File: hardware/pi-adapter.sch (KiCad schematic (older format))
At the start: 32 parts, among them P1 CONN_01X04, P10 CONN_01X04, P11 CONN_01X04, P12 CONN_01X04, P13 CONN_01X04, P14 CONN_01X04, P15 CONN_01X04, P16 CONN_01X04, P2 CONN_01X04, P20 CONN_02X20, P21 CONN_01X03, P22 CONN_01X06, P23 CONN_01X03, P3 CONN_01X04, P30 +5V, P31 GND, P4 CONN_01X04, P5 CONN_01X04, P6 CONN_01X04, P7 CONN_01X04, P8 CONN_01X04, P9 CONN_01X04, U1 74HCT245, U2 74HCT245, U3 74HCT245, U4 74HCT245

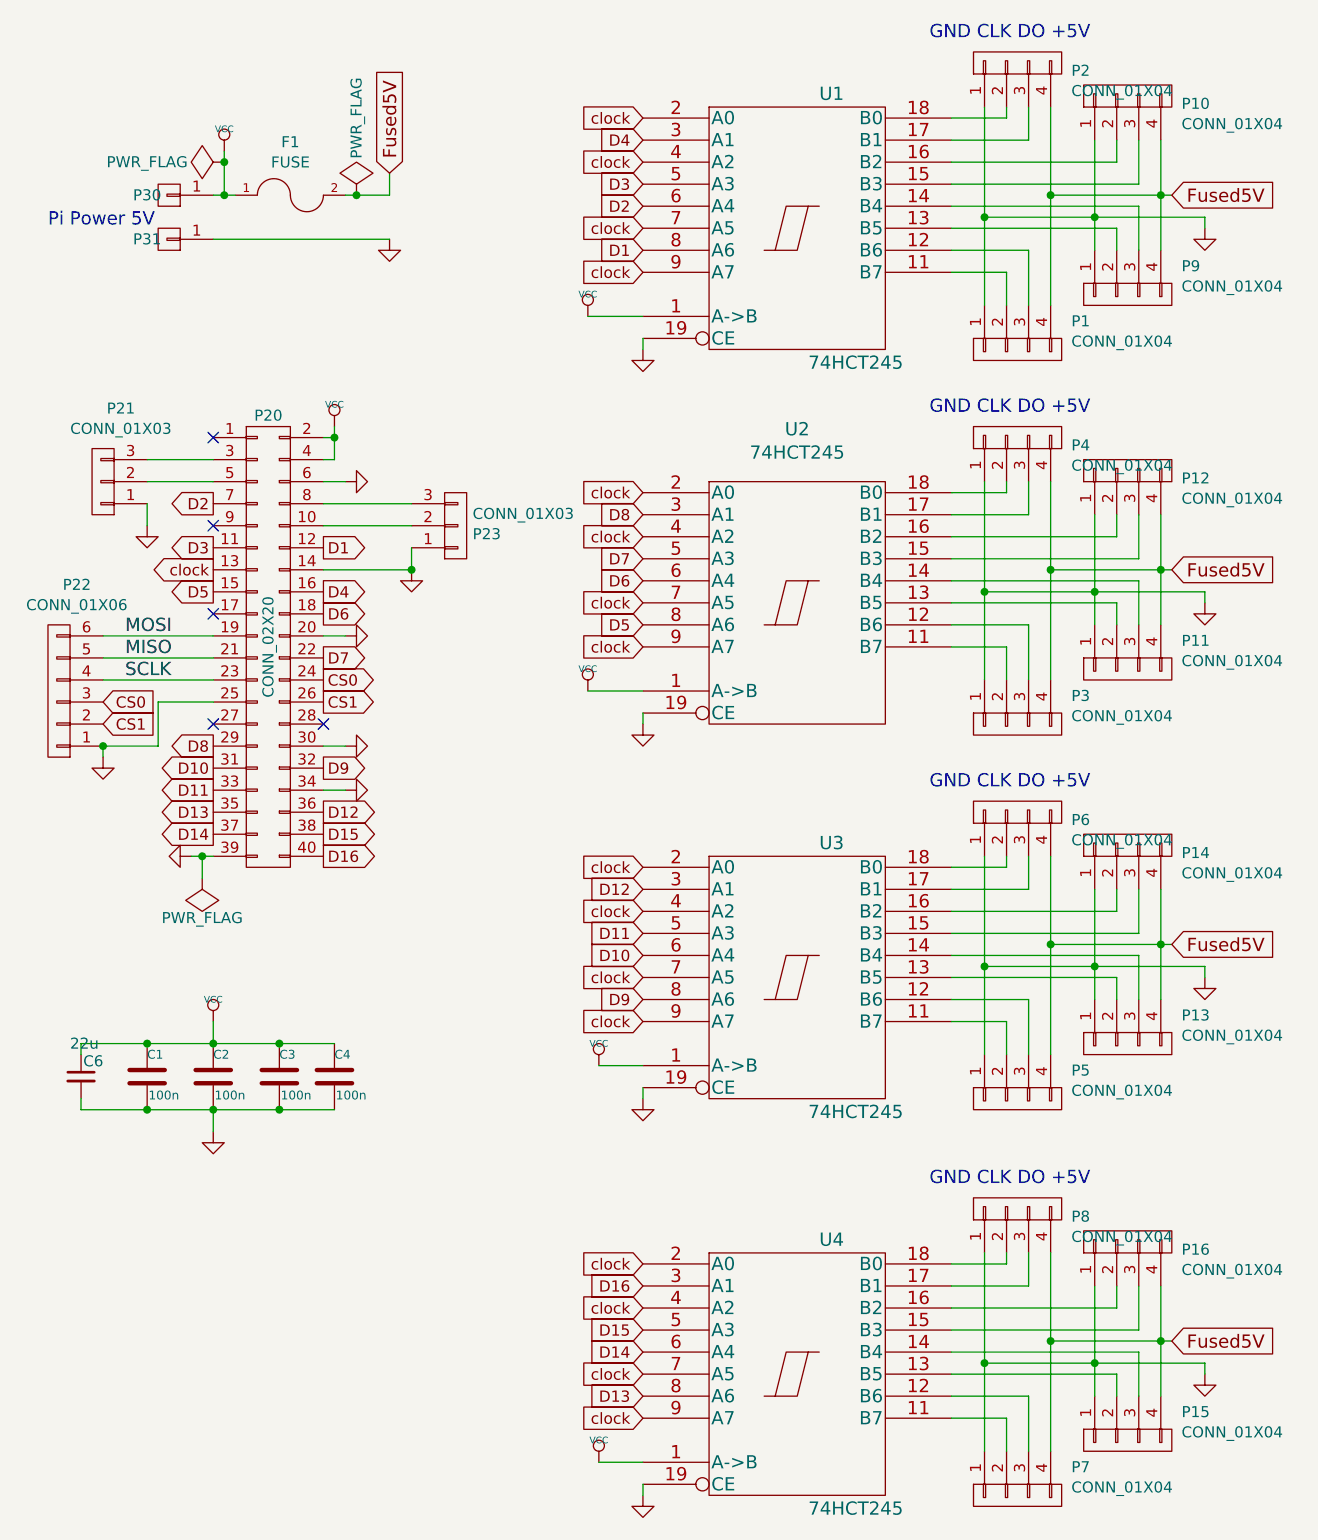
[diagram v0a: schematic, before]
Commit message: Add Schematic image in hardware/README.md
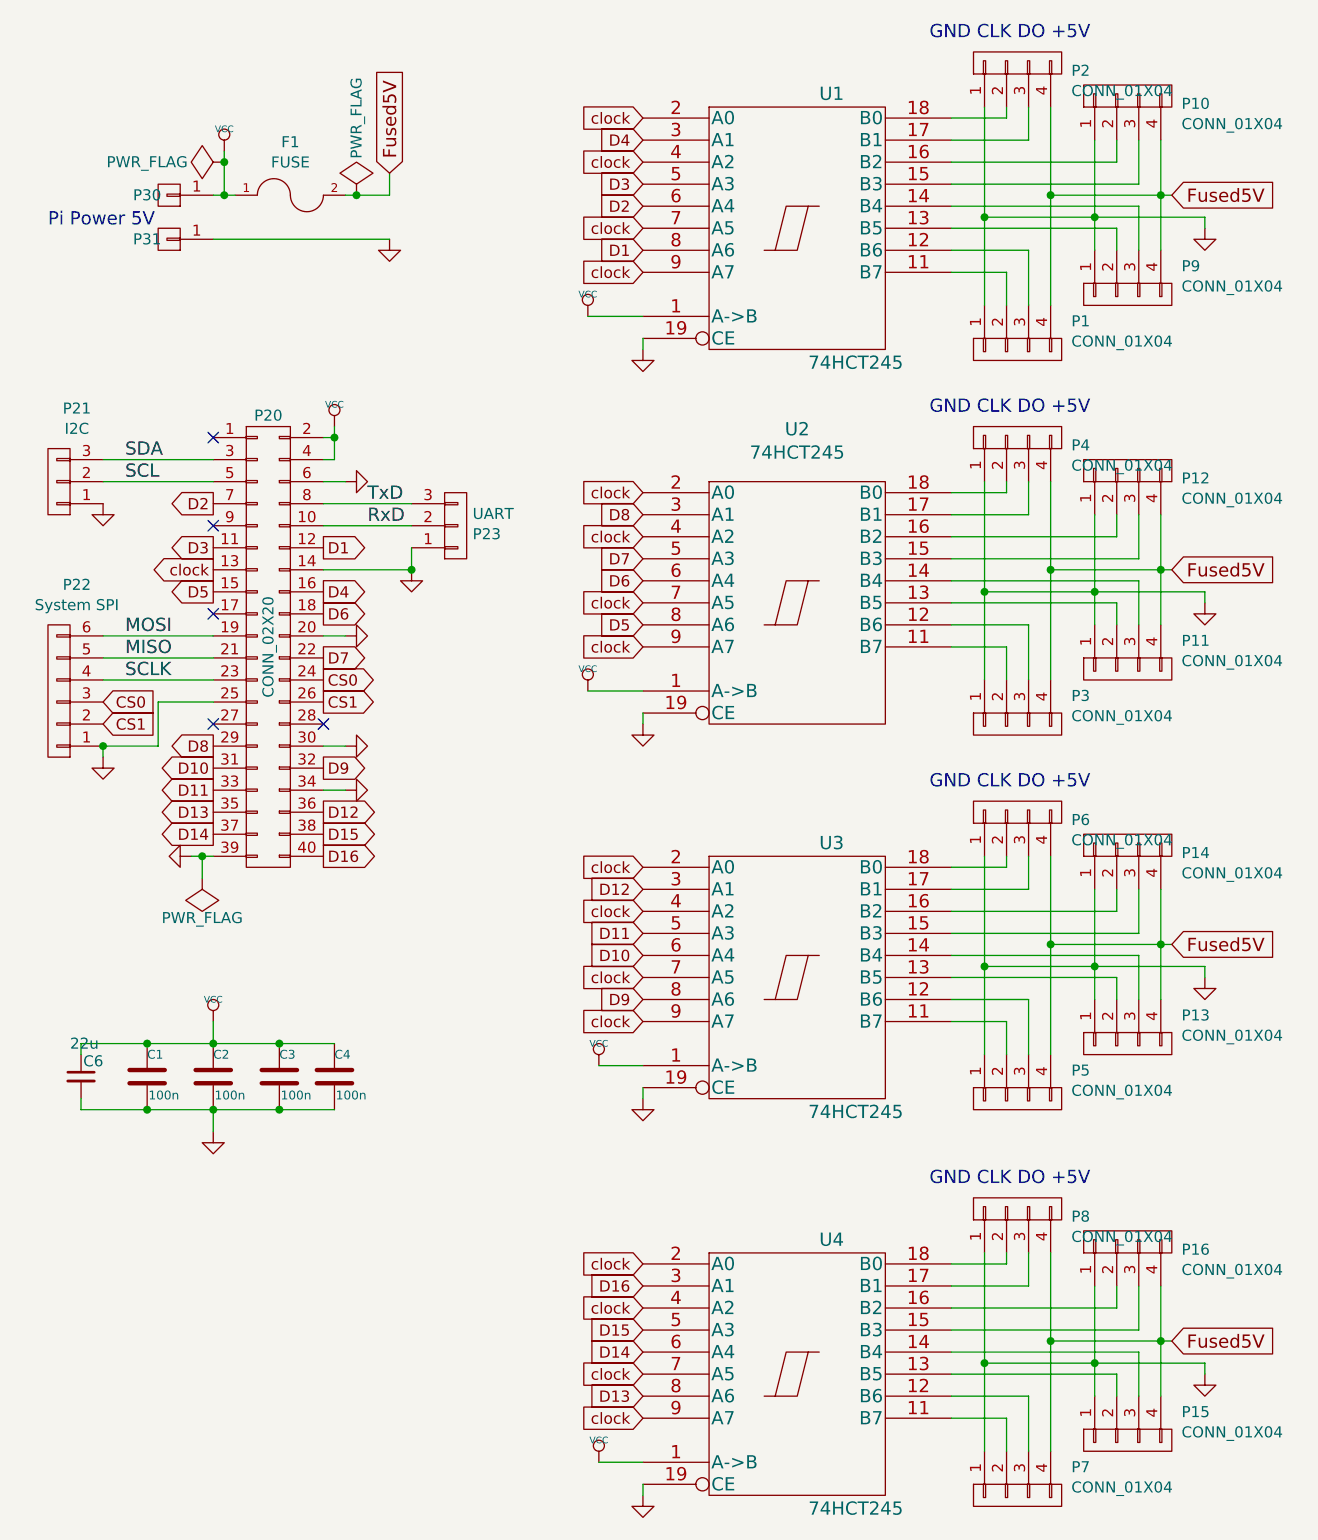
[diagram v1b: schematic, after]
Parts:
- P21: value CONN_01X03 -> I2C
- P22: value CONN_01X06 -> System SPI
- P23: value CONN_01X03 -> UART
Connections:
- net RxD: now reaches P20.10 (P10), P23.2 (P2)
- net SDA: now reaches P20.3 (P3), P21.3 (P3)
- net SCL: now reaches P20.5 (P5), P21.2 (P2)
- net TxD: now reaches P20.8 (P8), P23.3 (P3)
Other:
- moved on the sheet: P21
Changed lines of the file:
@@
 EESchema Schematic File Version 2
 LIBS:power
-LIBS:device
-LIBS:transistors
 LIBS:conn
-LIBS:linear
-LIBS:regul
 LIBS:74xx
-LIBS:cmos4000
-LIBS:adc-dac
-LIBS:memory
-LIBS:xilinx
-LIBS:microcontrollers
-LIBS:dsp
-LIBS:microchip
-LIBS:analog_switches
-LIBS:motorola
-LIBS:texas
-LIBS:intel
-LIBS:audio
-LIBS:interface
-LIBS:digital-audio
-LIBS:philips
-LIBS:display
-LIBS:cypress
-LIBS:siliconi
-LIBS:opto
-LIBS:atmel
-LIBS:contrib
-LIBS:valves
 LIBS:pi-adapter-cache
-EELAYER 25 0
+EELAYER 26 0
 EELAYER END
 $Descr A4 11693 8268
@@
 $EndComp
 Wire Wire Line
-	2450 2650 2450 2800
+	2450 2650 2450 2700
+Wire Wire Line
+	2450 2700 2450 2800
 Wire Wire Line
 	2450 2800 2400 2800
@@
 $EndComp
 Wire Wire Line
-	1800 4600 1900 4600
+	1800 4600 1850 4600
+Wire Wire Line
+	1850 4600 1900 4600
 $Comp
 L GND #PWR04
@@
 	1900 5450 1900 5350
 Wire Wire Line
-	1300 5450 2450 5450
+	1300 5450 1600 5450
+Wire Wire Line
+	1600 5450 1900 5450
+Wire Wire Line
+	1900 5450 2200 5450
+Wire Wire Line
+	2200 5450 2450 5450
 Connection ~ 1900 5450
 Wire Wire Line
-	1300 5750 2450 5750
+	1300 5750 1600 5750
+Wire Wire Line
+	1600 5750 1900 5750
+Wire Wire Line
+	1900 5750 2200 5750
+Wire Wire Line
+	2200 5750 2450 5750
 Connection ~ 1900 5750
 $Comp
@@
 	6100 1650 6100 1850
 Wire Wire Line
-	5400 1200 5400 2100
-Wire Wire Line
-	5900 1350 5900 1850
+	5400 1200 5400 1700
+Wire Wire Line
+	5400 1700 5400 2100
+Wire Wire Line
+	5900 1350 5900 1700
+Wire Wire Line
+	5900 1700 5900 1850
 $Comp
 L GND #PWR019
@@
 P 3000 3100
 F 0 "P23" H 3077 3138 50  0000 L CNN
-F 1 "CONN_01X03" H 3077 3046 50  0000 L CNN
+F 1 "UART" H 3077 3046 50  0000 L CNN
 F 2 "Pin_Headers:Pin_Header_Straight_1x03" H 3000 3100 50  0001 C CNN
 F 3 "" H 3000 3100 50  0000 C CNN
@@
 L CONN_01X03 P21
 U 1 1 56C19AA9
-P 1400 2900
-F 0 "P21" H 1319 2568 50  0000 C CNN
-F 1 "CONN_01X03" H 1319 2660 50  0000 C CNN
-F 2 "Pin_Headers:Pin_Header_Straight_1x03" H 1400 2900 50  0001 C CNN
-F 3 "" H 1400 2900 50  0000 C CNN
-	1    1400 2900
+P 1200 2900
+F 0 "P21" H 1119 2568 50  0000 C CNN
+F 1 "I2C" H 1119 2660 50  0000 C CNN
+F 2 "Pin_Headers:Pin_Header_Straight_1x03" H 1200 2900 50  0001 C CNN
+F 3 "" H 1200 2900 50  0000 C CNN
+	1    1200 2900
 	-1   0    0    1
 $EndComp
 Wire Wire Line
-	1600 2800 1900 2800
-Wire Wire Line
-	1600 2900 1900 2900
-$Comp
-L GND #PWR021
-U 1 1 56C19EE1
-P 1600 3100
-F 0 "#PWR021" H 1600 3100 30  0001 C CNN
-F 1 "GND" H 1600 3030 30  0001 C CNN
-F 2 "" H 1600 3100 60  0000 C CNN
-F 3 "" H 1600 3100 60  0000 C CNN
-	1    1600 3100
-	1    0    0    -1
-$EndComp
+	1400 2800 1900 2800
+Wire Wire Line
+	1400 2900 1900 2900
 Text GLabel 2400 3700 2    51   Output ~ 0
 D7
@@
 $EndComp
 Wire Wire Line
-	1900 1600 2000 1600
+	1900 1600 1950 1600
+Wire Wire Line
+	1950 1600 2000 1600
 Connection ~ 1950 1600
 $Comp
@@
 Connection ~ 1600 5750
 Wire Wire Line
-	2500 1600 2700 1600
+	2500 1600 2550 1600
+Wire Wire Line
+	2550 1600 2700 1600
 Wire Wire Line
 	1900 1800 2700 1800
@@
 	5600 1850 5600 2100
 Wire Wire Line
-	5700 1200 5700 2100
-Wire Wire Line
-	6200 1350 6200 1850
-Wire Wire Line
-	5700 1600 6250 1600
+	5700 1200 5700 1600
+Wire Wire Line
+	5700 1600 5700 2100
+Wire Wire Line
+	6200 1350 6200 1600
+Wire Wire Line
+	6200 1600 6200 1850
+Wire Wire Line
+	5700 1600 6200 1600
+Wire Wire Line
+	6200 1600 6250 1600
 Connection ~ 6200 1600
 Connection ~ 5700 1600
 Wire Wire Line
-	5400 1700 6400 1700
+	5400 1700 5900 1700
+Wire Wire Line
+	5900 1700 6400 1700
 Connection ~ 5900 1700
 Connection ~ 5400 1700
@@
 	6100 3350 6100 3550
 Wire Wire Line
-	5400 2900 5400 3800
-Wire Wire Line
-	5900 3050 5900 3550
+	5400 2900 5400 3400
+Wire Wire Line
+	5400 3400 5400 3800
+Wire Wire Line
+	5900 3050 5900 3400
+Wire Wire Line
+	5900 3400 5900 3550
 $Comp
 L GND #PWR023
@@
 	5600 3550 5600 3800
 Wire Wire Line
-	5700 2900 5700 3800
-Wire Wire Line
-	6200 3050 6200 3550
-Wire Wire Line
-	5700 3300 6250 3300
+	5700 2900 5700 3300
+Wire Wire Line
+	5700 3300 5700 3800
+Wire Wire Line
+	6200 3050 6200 3300
+Wire Wire Line
+	6200 3300 6200 3550
+Wire Wire Line
+	5700 3300 6200 3300
+Wire Wire Line
+	6200 3300 6250 3300
 Connection ~ 6200 3300
 Connection ~ 5700 3300
 Wire Wire Line
-	5400 3400 6400 3400
+	5400 3400 5900 3400
+Wire Wire Line
+	5900 3400 6400 3400
 Connection ~ 5900 3400
 Connection ~ 5400 3400
@@
 	6100 5050 6100 5250
 Wire Wire Line
-	5400 4600 5400 5500
-Wire Wire Line
-	5900 4750 5900 5250
+	5400 4600 5400 5100
+Wire Wire Line
+	5400 5100 5400 5500
+Wire Wire Line
+	5900 4750 5900 5100
+Wire Wire Line
+	5900 5100 5900 5250
 $Comp
 L GND #PWR024
@@
 	5600 5250 5600 5500
 Wire Wire Line
-	5700 4600 5700 5500
-Wire Wire Line
-	6200 4750 6200 5250
-Wire Wire Line
-	5700 5000 6250 5000
+	5700 4600 5700 5000
+Wire Wire Line
+	5700 5000 5700 5500
+Wire Wire Line
+	6200 4750 6200 5000
+Wire Wire Line
+	6200 5000 6200 5250
+Wire Wire Line
+	5700 5000 6200 5000
+Wire Wire Line
+	6200 5000 6250 5000
 Connection ~ 6200 5000
 Connection ~ 5700 5000
 Wire Wire Line
-	5400 5100 6400 5100
+	5400 5100 5900 5100
+Wire Wire Line
+	5900 5100 6400 5100
 Connection ~ 5900 5100
 Connection ~ 5400 5100
@@
 	6100 6850 6100 7050
 Wire Wire Line
-	5400 6400 5400 7300
-Wire Wire Line
-	5900 6550 5900 7050
+	5400 6400 5400 6900
+Wire Wire Line
+	5400 6900 5400 7300
+Wire Wire Line
+	5900 6550 5900 6900
+Wire Wire Line
+	5900 6900 5900 7050
 $Comp
 L GND #PWR025
@@
 	5600 7050 5600 7300
 Wire Wire Line
-	5700 6400 5700 7300
-Wire Wire Line
-	6200 6550 6200 7050
-Wire Wire Line
-	5700 6800 6250 6800
+	5700 6400 5700 6800
+Wire Wire Line
+	5700 6800 5700 7300
+Wire Wire Line
+	6200 6550 6200 6800
+Wire Wire Line
+	6200 6800 6200 7050
+Wire Wire Line
+	5700 6800 6200 6800
+Wire Wire Line
+	6200 6800 6250 6800
 Connection ~ 6200 6800
 Connection ~ 5700 6800
 Wire Wire Line
-	5400 6900 6400 6900
+	5400 6900 5900 6900
+Wire Wire Line
+	5900 6900 6400 6900
 Connection ~ 5900 6900
 Connection ~ 5400 6900
@@
 P 1200 3850
 F 0 "P22" H 1119 3368 50  0000 C CNN
-F 1 "CONN_01X06" H 1119 3460 50  0000 C CNN
+F 1 "System SPI" H 1119 3460 50  0000 C CNN
 F 2 "Pin_Headers:Pin_Header_Straight_1x06" H 1119 3460 50  0001 C CNN
 F 3 "" H 1200 3850 50  0000 C CNN
@@
 Connection ~ 2550 1600
 Wire Wire Line
-	1950 1400 1950 1600
+	1950 1400 1950 1450
+Wire Wire Line
+	1950 1450 1950 1600
 $Comp
 L PWR_FLAG #FLG027
@@
 Wire Wire Line
 	2400 3100 2800 3100
-Wire Wire Line
-	1600 3100 1600 3000
 NoConn ~ 1900 3100
+Text Label 1500 2800 0    60   ~ 0
+SDA
+Text Label 1500 2900 0    60   ~ 0
+SCL
+Text Label 2600 3000 0    60   ~ 0
+TxD
+Text Label 2600 3100 0    60   ~ 0
+RxD
+$Comp
+L GND #PWR?
+U 1 1 5934A175
+P 1400 3000
+F 0 "#PWR?" H 1400 3000 30  0001 C CNN
+F 1 "GND" H 1400 2930 30  0001 C CNN
+F 2 "" H 1400 3000 60  0000 C CNN
+F 3 "" H 1400 3000 60  0000 C CNN
+	1    1400 3000
+	1    0    0    -1
+$EndComp
 $EndSCHEMATC
